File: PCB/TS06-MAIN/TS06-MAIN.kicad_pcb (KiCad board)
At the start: 2 copper layers, 176 x 96 mm, 154 parts, among them J1 PH 6, U1 Arduino Nano, U10 TLP627, U11 TC4420, U12 LM393, U13 DS3231SN, U14 R-78E5.0-1.0, U2 K155ID1, U3 MCP23017, U4 MCP23017, U5 TLP627, U6 TLP627, U7 TLP627, U8 TLP627, U9 TLP627

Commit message: PCB: route TS06-MAIN; the router learns what has to be laid before what
The surface-mount build routes: 3047 tracks, 476 vias, every net connected except one
base pin. KiCad's own DRC with zones refilled reports 17 items, of which 2 are that net
and the rest are accepted (the tubes' pip holes inside their own courtyards, four
silkscreen warnings, the colon lamps touching the M10 glass courtyard by 0.3 mm).
checkmatch agrees the board and its schematic connect the same things.

ROUTING ORDER is the whole of it, and most of this diff is the evidence. Stages are now:
high voltage including the 185 V trunk, then GND as a tree, then everything else
negotiated, then one more try alone at whatever was dropped. What was tried and is worse
is written into tools/mkpcb_main.py beside each decision, with the numbers:

  * GND negotiated with the signals - it is 74 of 483 pads, so nearly every net is
    reported as overlapping GND rather than its real neighbour; two runs stuck at ~80 of
    98 nets overlapping and could not converge.
  * GND as a pour with stubs - the signal copper cuts the pour into islands; one region
    reached 37 of 74 pads and 66 stubs could not close the rest.
  * GND after the signals - the board is full by then; 21 pads unreachable, GND in
    11 pieces. Before them it wires with 0 or 1 connection missing.
  * The cathode spine laid first like the trunk - laid net after net it fences the rest
    in: 6 nets dropped instead of 3. Negotiation beats ordering, as TS06-SEC says.
  * AM/PM switches moved out of the tube rings - their 18 collectors then come back in
    through the ring edge with 0.6 mm halos and choke it: 24 nets dropped, and 13 when
    only the three with stranded pins were moved.

tools/pcbroute.py: negotiate() keeps its BEST round, not its last. price * cnt * (1 +
hist) saturates the int32 cap once the price has climbed far enough, and from there the
cost landscape is flat and the count wanders upward - 11, 12, 13, 17 over four rounds on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
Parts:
- BT1: footprint TS06_BatteryHolder_3034_Back_R90 -> TS06_BatteryHolder_3034_Back
- U3, U4: footprint TS06_SOIC-28W_Back -> TS06_SOIC-28W_Back_R90
- moved ? 186.1 mm to (6.00, 90.0)
- moved ? 165.0 mm to (170.0, 90.0)
- moved ? 81.0 mm to (90.0, 89.5)
- moved R10 70.9 mm to (127.2, 74.9)
- moved R11 70.9 mm to (129.8, 74.9)
- moved R12 70.9 mm to (132.2, 74.9)
- moved R13 70.9 mm to (134.8, 74.9)
- moved R14 70.9 mm to (137.2, 74.9)
- moved R15 70.9 mm to (139.8, 74.9)
- moved ? 70.1 mm to (83.0, 22.0)
- moved VT19 66.7 mm to (169.5, 62.3)
- moved R16 63.1 mm to (142.2, 74.9)
- moved R17 63.1 mm to (144.8, 74.9)
- moved R18 63.1 mm to (147.2, 74.9)
- moved R19 63.1 mm to (149.8, 74.9)
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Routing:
- net GND: track 0.00 -> 781.6 mm, vias 0 -> 57
- net +5V: track 0.00 -> 464.5 mm, vias 0 -> 44
- net HV185: track 0.00 -> 319.8 mm, vias 0 -> 12
- net SCL: track 0.00 -> 272.3 mm, vias 0 -> 14
- net SDA: track 0.00 -> 242.9 mm, vias 0 -> 12
- net K7: track 0.00 -> 199.7 mm, vias 0 -> 11
- net BL_K: track 0.00 -> 189.4 mm, vias 0 -> 16
- net K1: track 0.00 -> 176.1 mm, vias 0 -> 9
- net K2: track 0.00 -> 169.8 mm, vias 0 -> 6
- net D12: track 0.00 -> 167.4 mm, vias 0 -> 9
- net K9: track 0.00 -> 165.1 mm, vias 0 -> 6
- net K3: track 0.00 -> 165.0 mm, vias 0 -> 7
- net K5: track 0.00 -> 158.7 mm, vias 0 -> 7
- net K8: track 0.00 -> 157.5 mm, vias 0 -> 11
- net K4: track 0.00 -> 157.0 mm, vias 0 -> 14
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- added copper zone on B.Cu, net GND
- added copper zone on F.Cu, net GND

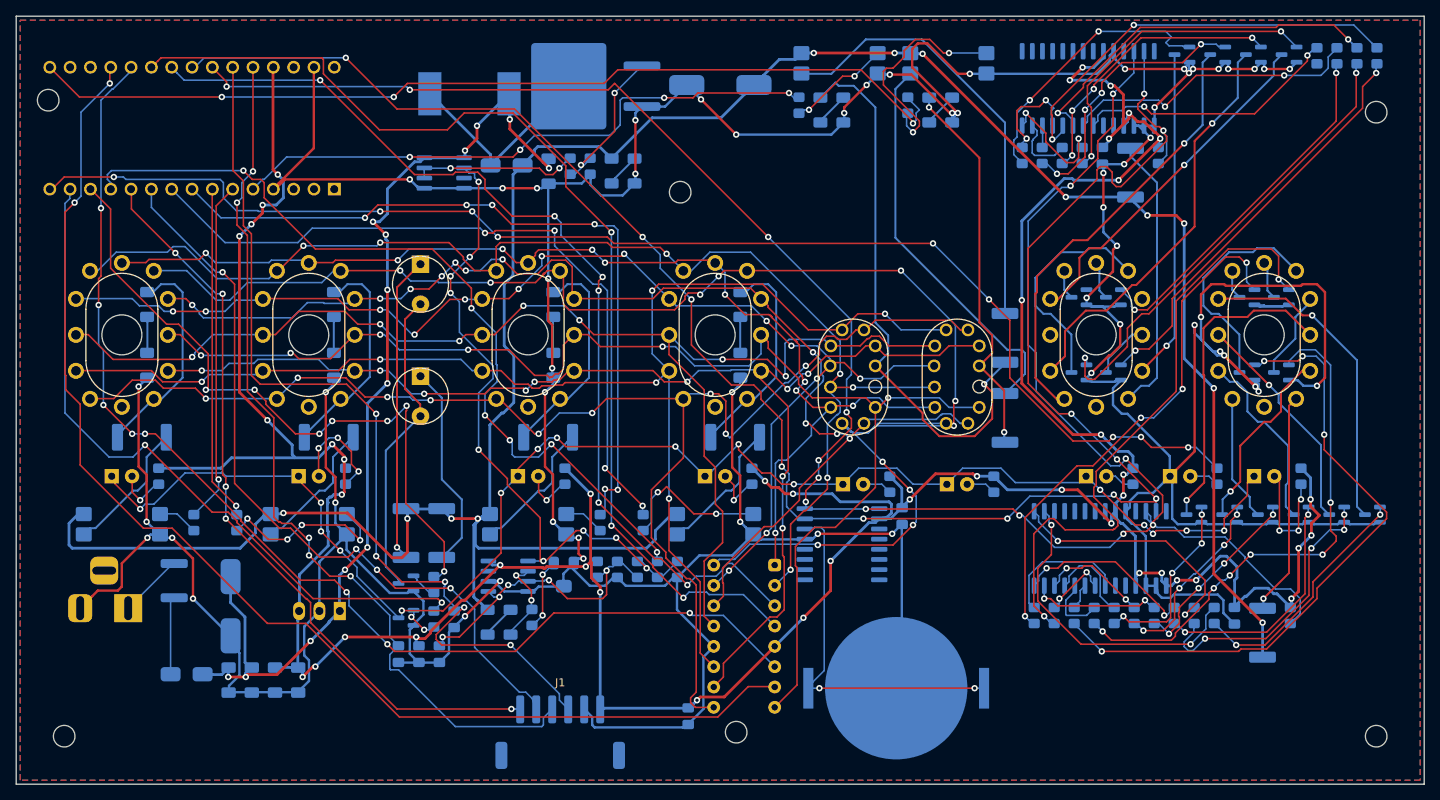
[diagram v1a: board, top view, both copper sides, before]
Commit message: TS06-MAIN: every signal net routed, 339 vias instead of 476, and an honest ground
The surface-mount board, re-routed with what the study settled on: grain 8, a via at
9 mm, relax 4, two tighten passes, history decay off, infrastructure nets exempt, and
a stage-4 rescue freed of the grain.

  every signal net routed   (the board that shipped left B2 split)
  339 vias                  (476)
  8726 mm of copper         (8575, at a 1.23x detour either way)
  49% / 11% front grain     (33% / 25% - that one is what routing at random looks like)
  checkcopper --hv clean, checkmatch agrees, audit down to one finding

The one finding is real and is NOT new. GND's copper joins into three pieces, not one:
VT10.2 and VT11.2 - the emitters of two ИН-15 cathode drivers - cannot be reached.
They sit among their own pins and the ИН-12 socket's 5 mm centre hole with gaps of
0.43 to 0.70 mm, and every escape leads into the socket's pin ring where the cathodes
need 0.6 mm. The pour does not reach them either.

This was in the board that shipped and in all twenty-two configurations tried today.
It was hidden by a bug in the stage-2 retry, which offered a stranded pad the three
nearest GND pads REGARDLESS OF WHETHER THEY WERE THEMSELVES CONNECTED: the two are
4.4 mm apart, each was offered the other, the connection succeeded, and both were
counted saved. audit.py had been reporting "GND is in 2 pieces" all along and I read
it as a fill prediction rather than as two floating emitters.

So the retry now only anchors on pads that actually reach the hub, and the routing log
prints how many pieces the COPPER ALONE joins GND into, before the pour is allowed any
credit, where it cannot be mistaken for a fill artefact. The count is honest now and
says three.

Fixing it needs the two transistors moved a half-millimetre off the socket, which is a
placement change in a block whose current arrangement is itself a measured decision -
moving these parts out of the tube rings was tried twice and cost 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
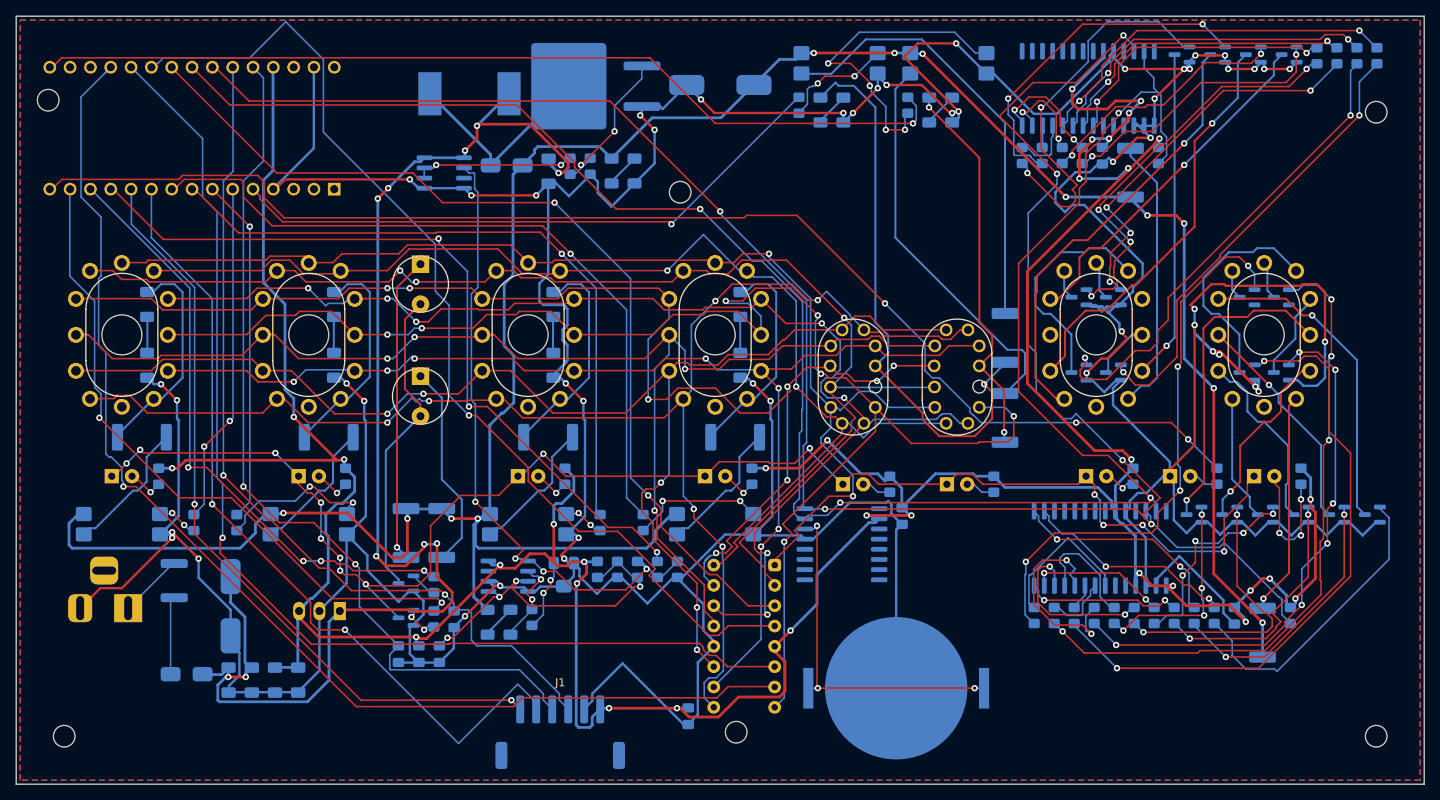
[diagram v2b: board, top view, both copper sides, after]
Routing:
- net GND: track 781.6 -> 837.2 mm, vias 57 -> 49
- net K7: track 199.7 -> 147.5 mm, vias 11 -> 2
- net B2: track 0.00 -> 52.0 mm, vias 0 -> 4
- net +12V: track 127.8 -> 167.3 mm, vias 13 -> 10
- net K9: track 165.1 -> 189.4 mm, vias 6 -> 7
- net +5V: track 464.5 -> 483.5 mm, vias 44 -> 31
- net U4_GPA3: track 8.10 -> 26.1 mm, vias 0 -> 2
- net B6: track 35.0 -> 49.5 mm
- net U4_GPB1: track 39.5 -> 26.9 mm
- net OPT_S1: track 28.3 -> 40.0 mm, vias 2 -> 4
- net B15: track 23.3 -> 34.9 mm, vias 4 -> 2
- net D5: track 94.3 -> 84.3 mm, vias 6 -> 1
- net BL_A2: track 14.0 -> 4.67 mm, vias 3 -> 1
- net D10: track 85.6 -> 76.4 mm, vias 7 -> 4
- net B7: track 34.5 -> 43.5 mm, vias 4 -> 2
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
